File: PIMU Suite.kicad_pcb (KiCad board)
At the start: 2 copper layers, 77 x 50.5 mm, 12 parts, among them J1 Conn_01x03, U1 Teensy4.1, U2 MICROSD_SPI_OR_SDIO_CARD

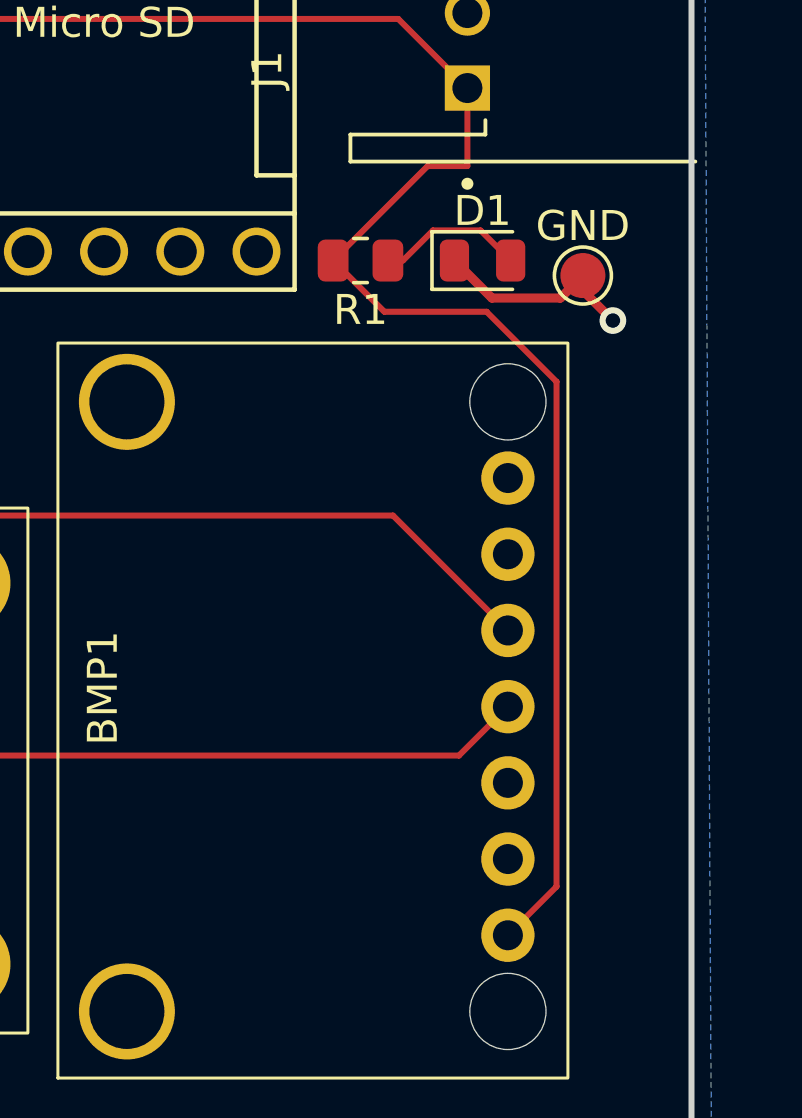
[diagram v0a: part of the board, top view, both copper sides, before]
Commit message: Haldsolder footprints
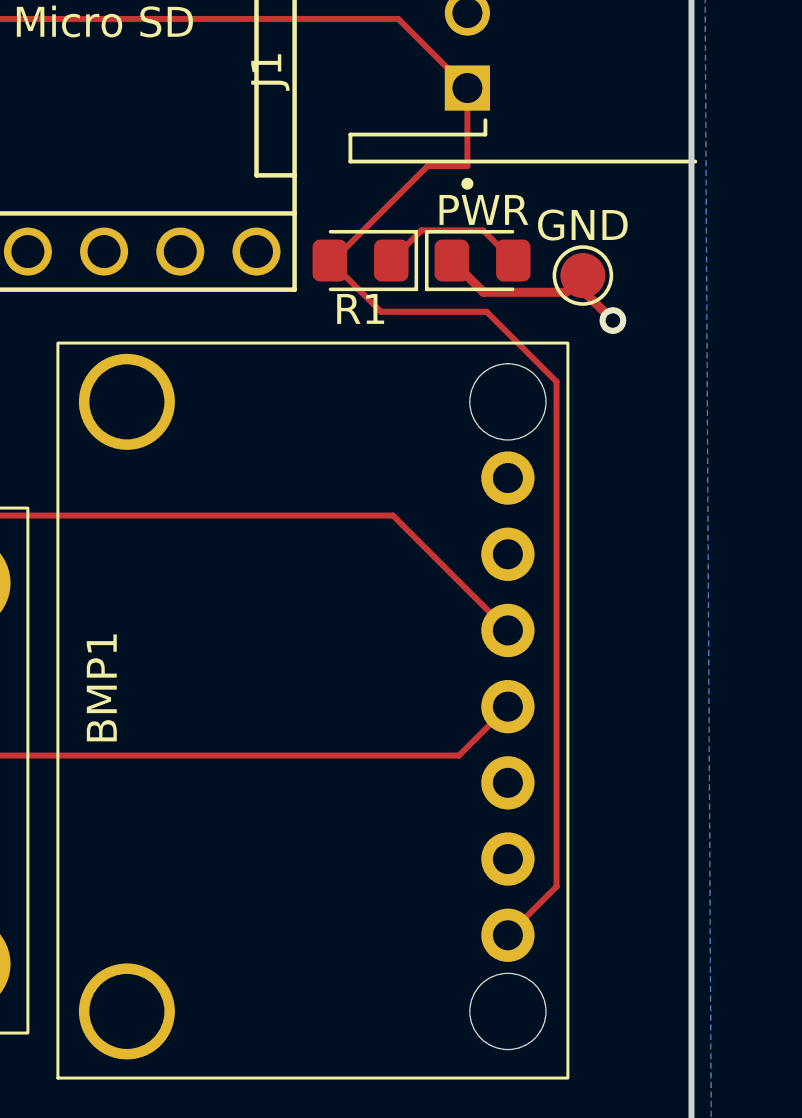
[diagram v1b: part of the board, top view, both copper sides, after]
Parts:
- PWR: renamed from D1; footprint LED_SMD:LED_0805_2012Metric -> LED_SMD:LED_0805_2012Metric_Pad1.15x1.40mm_HandSolder
- R1: footprint Resistor_SMD:R_0805_2012Metric -> LED_SMD:LED_0805_2012Metric_Pad1.15x1.40mm_HandSolder
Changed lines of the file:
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@@
 		(embedded_fonts no)
 	)
-	(footprint "LED_SMD:LED_0805_2012Metric"
+	(footprint "LED_SMD:LED_0805_2012Metric_Pad1.15x1.40mm_HandSolder"
 		(layer "F.Cu")
 		(at 176.155 94)
 		(descr "LED SMD 0805 (2012 Metric), square (rectangular) end terminal, IPC-7351 nominal, (Body size source: https://docs.google.com/spreadsheets/d/1BsfQQcO9C6DZCsRaXUlFlo91Tg2WpOkGARC1WS5S8t0/edit?usp=sharing), generated with kicad-footprint-generator")
-		(tags "LED")
-		(property "Reference" "D1"
+		(tags "LED handsolder")
+		(property "Reference" "PWR"
 			(at 0 -1.65 0)
 			(layer "F.SilkS")
@@
 		(attr smd)
 		(fp_line
-			(start -1.685 -0.96)
-			(end -1.685 0.96)
+			(start -1.86 -0.96)
+			(end -1.86 0.96)
 			(stroke
 				(width 0.12)
@@
 		)
 		(fp_line
-			(start -1.685 0.96)
+			(start -1.86 0.96)
 			(end 1 0.96)
 			(stroke
@@
 		(fp_line
 			(start 1 -0.96)
-			(end -1.685 -0.96)
+			(end -1.86 -0.96)
 			(stroke
 				(width 0.12)
@@
 		)
 		(fp_line
-			(start -1.68 -0.95)
-			(end 1.68 -0.95)
+			(start -1.85 -0.95)
+			(end 1.85 -0.95)
 			(stroke
 				(width 0.05)
@@
 		)
 		(fp_line
-			(start -1.68 0.95)
-			(end -1.68 -0.95)
+			(start -1.85 0.95)
+			(end -1.85 -0.95)
 			(stroke
 				(width 0.05)
@@
 		)
 		(fp_line
-			(start 1.68 -0.95)
-			(end 1.68 0.95)
+			(start 1.85 -0.95)
+			(end 1.85 0.95)
 			(stroke
 				(width 0.05)
@@
 		)
 		(fp_line
-			(start 1.68 0.95)
-			(end -1.68 0.95)
+			(start 1.85 0.95)
+			(end -1.85 0.95)
 			(stroke
 				(width 0.05)
@@
 		)
 		(pad "1" smd roundrect
-			(at -0.9375 0)
-			(size 0.975 1.4)
+			(at -1.025 0)
+			(size 1.15 1.4)
 			(layers "F.Cu" "F.Mask" "F.Paste")
-			(roundrect_rratio 0.25)
+			(roundrect_rratio 0.217391)
 			(net 35 "GND")
 			(pinfunction "K")
@@
 		)
 		(pad "2" smd roundrect
-			(at 0.9375 0)
-			(size 0.975 1.4)
+			(at 1.025 0)
+			(size 1.15 1.4)
 			(layers "F.Cu" "F.Mask" "F.Paste")
-			(roundrect_rratio 0.25)
+			(roundrect_rratio 0.217391)
 			(net 81 "Net-(D1-A)")
 			(pinfunction "A")
@@
 		(embedded_fonts no)
 	)
-	(footprint "Resistor_SMD:R_0805_2012Metric"
+	(footprint "LED_SMD:LED_0805_2012Metric_Pad1.15x1.40mm_HandSolder"
 		(layer "F.Cu")
 		(at 172.0875 94 180)
-		(descr "Resistor SMD 0805 (2012 Metric), square (rectangular) end terminal, IPC-7351 nominal, (Body size source: IPC-SM-782 page 72, https://www.pcb-3d.com/wordpress/wp-content/uploads/ipc-sm-782a_amendment_1_and_2.pdf), generated with kicad-footprint-generator")
-		(tags "resistor")
+		(descr "LED SMD 0805 (2012 Metric), square (rectangular) end terminal, IPC-7351 nominal, (Body size source: https://docs.google.com/spreadsheets/d/1BsfQQcO9C6DZCsRaXUlFlo91Tg2WpOkGARC1WS5S8t0/edit?usp=sharing), generated with kicad-footprint-generator")
+		(tags "LED handsolder")
 		(property "Reference" "R1"
 			(at 0 -1.65 180)
@@
 		(attr smd)
 		(fp_line
-			(start -0.227064 0.735)
-			(end 0.227064 0.735)
+			(start 1 -0.96)
+			(end -1.86 -0.96)
 			(stroke
 				(width 0.12)
@@
 		)
 		(fp_line
-			(start -0.227064 -0.735)
-			(end 0.227064 -0.735)
+			(start -1.86 0.96)
+			(end 1 0.96)
 			(stroke
 				(width 0.12)
@@
 		)
 		(fp_line
-			(start 1.68 0.95)
-			(end -1.68 0.95)
+			(start -1.86 -0.96)
+			(end -1.86 0.96)
+			(stroke
+				(width 0.12)
+				(type solid)
+			)
+			(layer "F.SilkS")
+		)
+		(fp_line
+			(start 1.85 0.95)
+			(end -1.85 0.95)
 			(stroke
 				(width 0.05)
@@
 		)
 		(fp_line
-			(start 1.68 -0.95)
-			(end 1.68 0.95)
+			(start 1.85 -0.95)
+			(end 1.85 0.95)
 			(stroke
 				(width 0.05)
@@
 		)
 		(fp_line
-			(start -1.68 0.95)
-			(end -1.68 -0.95)
+			(start -1.85 0.95)
+			(end -1.85 -0.95)
 			(stroke
 				(width 0.05)
@@
 		)
 		(fp_line
-			(start -1.68 -0.95)
-			(end 1.68 -0.95)
+			(start -1.85 -0.95)
+			(end 1.85 -0.95)
 			(stroke
 				(width 0.05)
@@
 		)
 		(fp_line
-			(start 1 0.625)
-			(end -1 0.625)
+			(start 1 0.6)
+			(end 1 -0.6)
+			(stroke
+				(width 0.1)
+				(type solid)
+			)
+			(layer "F.Fab")
+		)
+		(fp_line
+			(start 1 -0.6)
+			(end -0.7 -0.6)
 			(stroke
 				(width 0.1)
@@
 		)
 		(fp_line
-			(start 1 -0.625)
-			(end 1 0.625)
+			(start -0.7 -0.6)
+			(end -1 -0.3)
 			(stroke
 				(width 0.1)
@@
 		)
 		(fp_line
-			(start -1 0.625)
-			(end -1 -0.625)
+			(start -1 0.6)
+			(end 1 0.6)
 			(stroke
 				(width 0.1)
@@
 		)
 		(fp_line
-			(start -1 -0.625)
-			(end 1 -0.625)
+			(start -1 -0.3)
+			(end -1 0.6)
 			(stroke
 				(width 0.1)
@@
 		)
 		(pad "1" smd roundrect
-			(at -0.9125 0 180)
-			(size 1.025 1.4)
+			(at -1.025 0 180)
+			(size 1.15 1.4)
 			(layers "F.Cu" "F.Mask" "F.Paste")
-			(roundrect_rratio 0.243902)
+			(roundrect_rratio 0.217391)
 			(net 81 "Net-(D1-A)")
 			(pintype "passive")
 		)
 		(pad "2" smd roundrect
-			(at 0.9125 0 180)
-			(size 1.025 1.4)
+			(at 1.025 0 180)
+			(size 1.15 1.4)
 			(layers "F.Cu" "F.Mask" "F.Paste")
-			(roundrect_rratio 0.243902)
+			(roundrect_rratio 0.217391)
 			(net 24 "+3.3V")
 			(pintype "passive")
 		)
 		(embedded_fonts no)
-		(model "${KICAD9_3DMODEL_DIR}/Resistor_SMD.3dshapes/R_0805_2012Metric.step"
+		(model "${KICAD9_3DMODEL_DIR}/LED_SMD.3dshapes/LED_0805_2012Metric.step"
 			(offset
 				(xyz 0 0 0)
@@
 	)
 	(segment
-		(start 178.621 114.869)
-		(end 178.621 98.03856)
+		(start 171.0625 94)
+		(end 171.175 94)
 		(width 0.2)
 		(layer "F.Cu")
@@
 	)
 	(segment
-		(start 178.621 98.03856)
-		(end 176.28904 95.7066)
+		(start 142.31 117.45)
+		(end 140.4042 115.5442)
 		(width 0.2)
 		(layer "F.Cu")
@@
 	)
 	(segment
-		(start 142.31 117.45)
-		(end 140.4042 115.5442)
+		(start 176.28904 95.7066)
+		(end 178.621 98.03856)
 		(width 0.2)
 		(layer "F.Cu")
@@
 	)
 	(segment
-		(start 172.8816 95.7066)
-		(end 171.175 94)
+		(start 178.621 114.869)
+		(end 177 116.49)
 		(width 0.2)
 		(layer "F.Cu")
@@
 	)
 	(segment
-		(start 177 116.49)
-		(end 178.621 114.869)
-		(width 0.2)
-		(layer "F.Cu")
-		(net 24)
-	)
-	(segment
 		(start 144.3242 94.1758)
 		(end 138.39 100.11)
@@
 	)
 	(segment
-		(start 176.28904 95.7066)
-		(end 172.8816 95.7066)
+		(start 172.7691 95.7066)
+		(end 176.28904 95.7066)
 		(width 0.2)
 		(layer "F.Cu")
@@
 	)
 	(segment
-		(start 178.75 95.25)
-		(end 179.5 94.5)
-		(width 0.3048)
+		(start 178.621 98.03856)
+		(end 178.621 114.869)
+		(width 0.2)
 		(layer "F.Cu")
-		(net 35)
+		(net 24)
+	)
+	(segment
+		(start 171.0625 94)
+		(end 172.7691 95.7066)
+		(width 0.2)
+		(layer "F.Cu")
+		(net 24)
 	)
 	(segment
@@
 	)
 	(segment
-		(start 176.4675 95.25)
-		(end 178.75 95.25)
+		(start 178.9434 95.0566)
+		(end 179.5 94.5)
+		(width 0.3048)
+		(layer "F.Cu")
+		(net 35)
+	)
+	(segment
+		(start 176.1866 95.0566)
+		(end 178.9434 95.0566)
 		(width 0.3048)
 		(layer "F.Cu")
@@
 	)
 	(segment
-		(start 175.2175 94)
-		(end 176.4675 95.25)
+		(start 175.13 94)
+		(end 176.1866 95.0566)
 		(width 0.3048)
 		(layer "F.Cu")
@@
 	)
 	(segment
-		(start 176.0883 92.9958)
-		(end 177.0925 94)
+		(start 174.1167 92.9958)
+		(end 173.1125 94)
 		(width 0.2)
 		(layer "F.Cu")
@@
 	)
 	(segment
-		(start 174.5042 92.9958)
-		(end 173.5 94)
+		(start 177.18 94)
+		(end 176.1758 92.9958)
 		(width 0.2)
 		(layer "F.Cu")
@@
 	)
 	(segment
-		(start 174.5042 92.9958)
-		(end 176.0883 92.9958)
+		(start 176.1758 92.9958)
+		(end 174.1167 92.9958)
 		(width 0.2)
 		(layer "F.Cu")

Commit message: Updates from team
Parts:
- removed J1: Conn_01x03, RSX:JST_S4B-XH-A-1
- added G***: LOGO, LOGO, F.Cu at (164.0, 108.0)
- added G***: LOGO, LOGO, F.Cu at (122.5, 117.5)
- added G***: LOGO, LOGO, F.Cu at (148.5, 108.0)
- added JST1: S4B-XH-A-1, Connector_JST:JST_VH_B3P-VH-B_1x03_P3.96mm_Vertical, F.Cu at (175.5, 88.4)
- R1: footprint LED_SMD:LED_0805_2012Metric_Pad1.15x1.40mm_HandSolder -> Resistor_SMD:R_0805_2012Metric_Pad1.20x1.40mm_HandSolder
- TP1: value 5V -> 5V IN
- TP2: renamed from GND; value GND CONN -> GND
- moved TP4 2.55 mm to (157.0, 100.0)
- renumbered PWR to D1, U1 to TEENSY1, SCL to TP3, SDA to TP4
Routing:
- net /SCL_LINE: track 58.9 -> 74.7 mm, vias 2 -> 0
- net +3.3V: track 106.7 -> 95.5 mm
- net /SDA_LINE: track 58.3 -> 60.9 mm
- net /SD_SCK: track 30.9 -> 28.3 mm
- net +5V: track 72.4 -> 74.3 mm
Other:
- board text added: "Micro SD"
- board text added: "x"

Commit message: Fix JST order
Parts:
- added G***: LOGO, LOGO, F.Cu at (110.0, 74.5)
- BMP1: value BMP280 Breakout -> BMP280
- TP2: value GND -> GND CONN
- moved JST1 7.68 mm to (177.5, 81.0), turned to -90 degrees
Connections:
- JST1 pad 1: +3.3V -> GND
- JST1 pad 3: GND -> +3.3V
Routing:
- net +3.3V: track 95.5 -> 96.6 mm
- net +5V: track 74.3 -> 73.4 mm

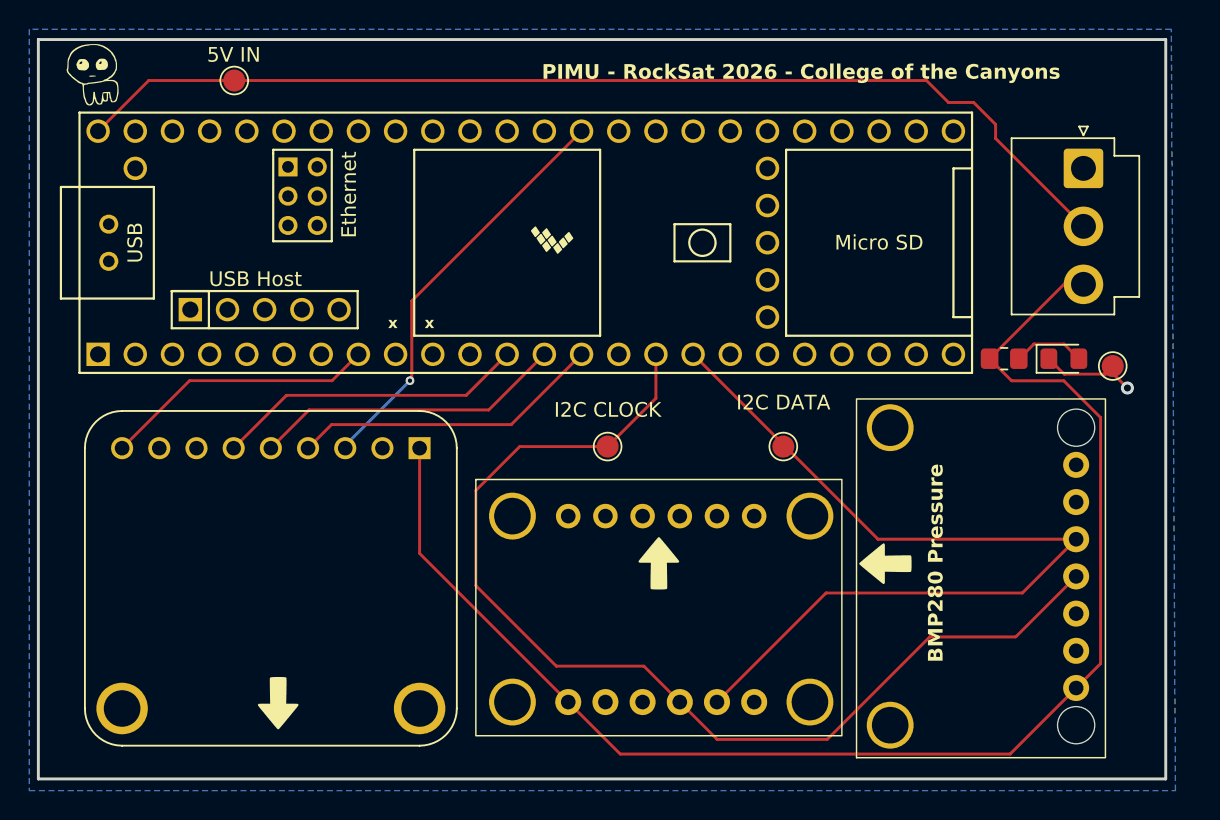
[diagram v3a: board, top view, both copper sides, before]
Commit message: Tweaked for manufactering
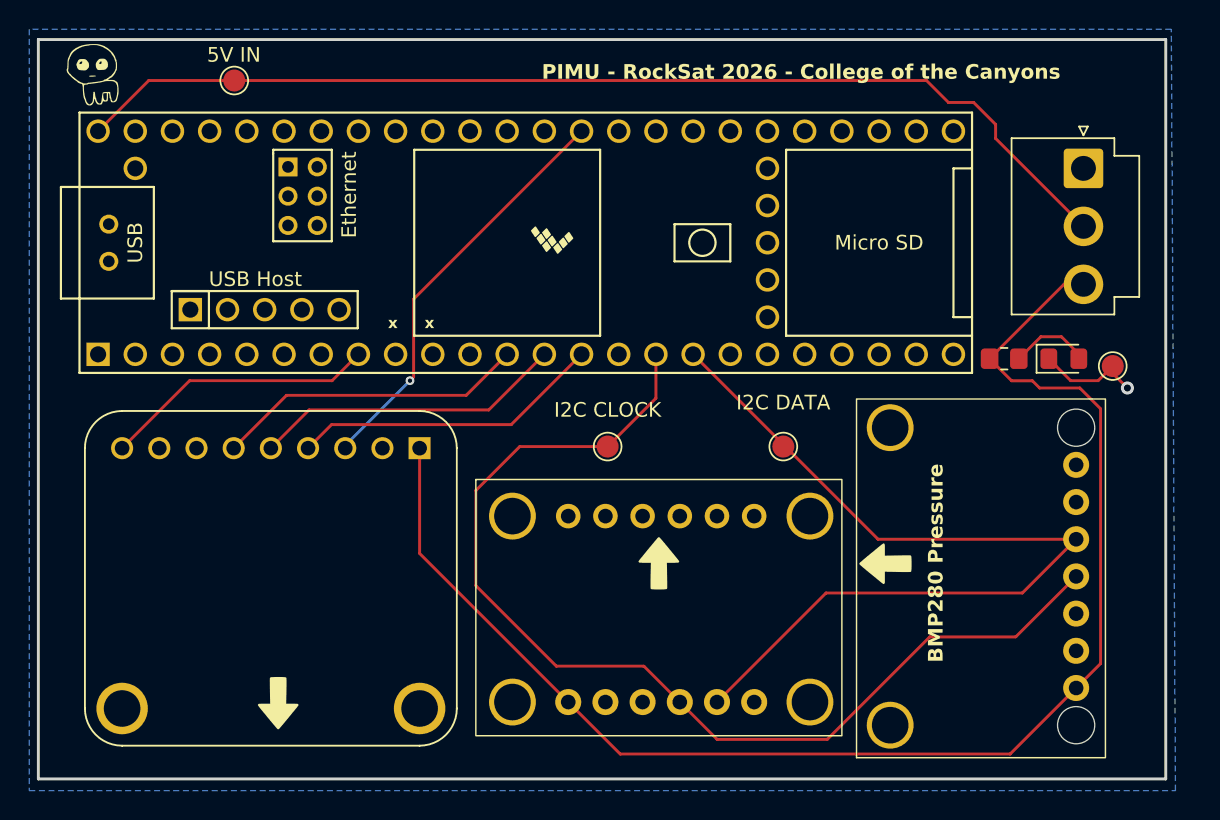
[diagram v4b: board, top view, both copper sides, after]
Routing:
- net Net-(D1-A): track 5.40 -> 6.02 mm
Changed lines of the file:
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@@
 	)
 	(segment
-		(start 131.6242 90.0558)
+		(start 131.5 95.5)
+		(end 131.75 95.25)
+		(width 0.2)
+		(layer "F.Cu")
+		(net 19)
+	)
+	(segment
+		(start 131.75 89.93)
 		(end 143.22 78.46)
 		(width 0.2)
@@
 	)
 	(segment
-		(start 131.5 95.5)
-		(end 131.6242 95.3758)
-		(width 0.2)
-		(layer "F.Cu")
-		(net 19)
-	)
-	(segment
-		(start 131.6242 95.3758)
-		(end 131.6242 90.0558)
+		(start 131.75 95.25)
+		(end 131.75 89.93)
 		(width 0.2)
 		(layer "F.Cu")
@@
 	)
 	(segment
-		(start 178.6685 98.018885)
-		(end 176.157915 95.5083)
+		(start 174.0083 95.5083)
+		(end 172.5958 95.5083)
 		(width 0.2)
 		(layer "F.Cu")
@@
 	)
 	(segment
+		(start 178.6685 97.4185)
+		(end 177.25 96)
+		(width 0.2)
+		(layer "F.Cu")
+		(net 24)
+	)
+	(segment
 		(start 132.16 107.3)
 		(end 142.31 117.45)
@@
 	)
 	(segment
-		(start 176.157915 95.5083)
-		(end 172.5958 95.5083)
+		(start 177 116.49)
+		(end 178.6685 114.8215)
 		(width 0.2)
 		(layer "F.Cu")
@@
 	)
 	(segment
+		(start 172.5958 95.5083)
+		(end 171.0875 94)
+		(width 0.2)
+		(layer "F.Cu")
+		(net 24)
+	)
+	(segment
+		(start 177.25 96)
+		(end 174.5 96)
+		(width 0.2)
+		(layer "F.Cu")
+		(net 24)
+	)
+	(segment
 		(start 178.6685 114.8215)
-		(end 178.6685 98.018885)
+		(end 178.6685 97.4185)
 		(width 0.2)
 		(layer "F.Cu")
@@
 	)
 	(segment
-		(start 177 116.49)
-		(end 178.6685 114.8215)
+		(start 174.5 96)
+		(end 174.0083 95.5083)
 		(width 0.2)
 		(layer "F.Cu")
@@
 	)
 	(segment
-		(start 172.5958 95.5083)
-		(end 171.0875 94)
-		(width 0.2)
-		(layer "F.Cu")
-		(net 24)
-	)
-	(segment
 		(start 116.45 95.5)
 		(end 126.18 95.5)
@@
 	)
 	(segment
-		(start 176.1866 95.0566)
-		(end 178.9434 95.0566)
-		(width 0.2)
-		(layer "F.Cu")
-		(net 35)
-	)
-	(segment
-		(start 178.9434 95.0566)
-		(end 179.5 94.5)
-		(width 0.3048)
+		(start 175.13 94)
+		(end 176.63 95.5)
+		(width 0.2)
 		(layer "F.Cu")
 		(net 35)
@@
 	)
 	(segment
-		(start 175.13 94)
-		(end 176.1866 95.0566)
+		(start 178.5 95.5)
+		(end 179.5 94.5)
+		(width 0.2)
+		(layer "F.Cu")
+		(net 35)
+	)
+	(segment
+		(start 176.63 95.5)
+		(end 178.5 95.5)
 		(width 0.2)
 		(layer "F.Cu")
@@
 	)
 	(segment
-		(start 174.1167 92.9958)
-		(end 173.1125 94)
+		(start 174.5875 92.5)
+		(end 176 92.5)
 		(width 0.2)
 		(layer "F.Cu")
@@
 	)
 	(segment
-		(start 177.18 94)
-		(end 176.1758 92.9958)
+		(start 173.0875 94)
+		(end 174.5875 92.5)
+		(width 0.2)
+		(layer "F.Cu")
+		(net 81)
+	)
+	(segment
+		(start 176 92.5)
+		(end 177.18 93.68)
 		(width 0.2)
 		(layer "F.Cu")
@@
 	)
 	(segment
-		(start 176.1758 92.9958)
-		(end 174.1167 92.9958)
-		(width 0.2)
-		(layer "F.Cu")
+		(start 177.18 93.68)
+		(end 177.18 94)
+		(width 0.2)
+		(layer "F.Cu")

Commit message: Update silk
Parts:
- R1: value R_US -> ~65Ω
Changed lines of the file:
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@@
 			(unlocked yes)
 			(layer "F.SilkS")
-			(hide yes)
 			(effects
 				(font
@@
 			)
 		)
-		(property "Description" ""
+		(property "Description" "ICM20649 IMU"
 			(at 0 2.75 0)
 			(unlocked yes)
@@
 			)
 		)
-		(property "Description" "Light emitting diode"
+		(property "Description" "PWR"
 			(at -0.155 2 0)
 			(layer "F.SilkS")
-			(hide yes)
 			(effects
 				(font
@@
 			)
 		)
-		(property "Description" ""
+		(property "Description" "SD Card Breakout"
 			(at 0 0 180)
 			(unlocked yes)
@@
 				(font
 					(size 1 1)
-					(thickness 0.15)
+					(thickness 0.2)
+					(bold yes)
 				)
 			)
@@
 			)
 		)
-		(property "Description" "test point"
-			(at 0 0 0)
+		(property "Description" "GND"
+			(at 1 -2 0)
 			(unlocked yes)
-			(layer "F.Fab")
-			(hide yes)
+			(layer "F.SilkS")
 			(effects
 				(font
 					(size 1.27 1.27)
-					(thickness 0.15)
+					(thickness 0.254)
+					(bold yes)
 				)
 			)
@@
 		)
 		(property "Value" "I2C DATA"
-			(at 0 -3 0)
+			(at 0 -2.5 0)
 			(layer "F.SilkS")
 			(effects
 				(font
 					(size 1 1)
-					(thickness 0.15)
+					(thickness 0.2)
+					(bold yes)
 				)
 			)
@@
 				(font
 					(size 1 1)
-					(thickness 0.15)
+					(thickness 0.2)
+					(bold yes)
 				)
 			)
@@
 			)
 		)
-		(property "Value" "R_US"
+		(property "Value" "~65Ω"
 			(at 0 1.65 180)
-			(layer "F.Fab")
-			(hide yes)
+			(layer "F.SilkS")
 			(effects
 				(font
 					(size 1 1)
-					(thickness 0.15)
+					(thickness 0.2)
+					(bold yes)
 				)
 			)
